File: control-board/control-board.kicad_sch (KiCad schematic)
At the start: 623 parts, among them J1 LED ch 1-24, J10 ESP32 left (3V3 row), J11 ESP32 right (GND row), J2 LED ch 25-48, J3 LED ch 49-72, J4 LED ch 73-96, J5 logic/analog, J6 24V IN, J7 24V IN (5.5/2.5), J8 FAN 24V, Q1 AO3400A, SW1 MODE, SW2 UP, SW3 DOWN, U1 PT4115, U10 PT4115, U101 PCA9685PW (0x40), U102 PCA9685PW (0x41), U103 PCA9685PW (0x42), U104 PCA9685PW (0x43), U105 PCA9685PW (0x44), U106 PCA9685PW (0x45), U11 PT4115, U110 XL1509-5.0E1, U111 ADS1115IDGS (DNP), U12 PT4115, U13 PT4115, U14 PT4115, U15 PT4115, U16 PT4115, U17 PT4115, U18 PT4115, U19 PT4115, U2 PT4115, U20 PT4115, U21 PT4115, U22 PT4115, U23 PT4115, U24 PT4115, U25 PT4115, U26 PT4115, U27 PT4115, U28 PT4115, U29 PT4115, U3 PT4115, U30 PT4115, U31 PT4115, U32 PT4115, U33 PT4115, U34 PT4115, U35 PT4115, U36 PT4115, U37 PT4115, U38 PT4115, U39 PT4115, U4 PT4115, U40 PT4115, U41 PT4115, U42 PT4115, U43 PT4115, U44 PT4115, U45 PT4115, U46 PT4115, U47 PT4115, U48 PT4115, U49 PT4115, U5 PT4115, U50 PT4115, U51 PT4115, U52 PT4115, U53 PT4115, U54 PT4115, U55 PT4115, U56 PT4115, U57 PT4115, U58 PT4115, U59 PT4115, U6 PT4115, U60 PT4115, U61 PT4115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

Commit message: Hierarchical schematics: fully wired, netlist-verified, ERC clean
- Root + well.kicad_sch / channel.kicad_sch instantiated 96x each;
  refs preserved (LED1-96, U1-96...) via instance paths
- Sub-sheets pre-wired; root connected via net labels; no_connects
  on unused ESP32 socket pins; PWR_FLAGs per rail
- verify_netlist.py: KiCad netlist export matches design_data on all
  300 (LED) + 412 (control) intended nets; ERC clean / 3 benign warns
- LCSC corrections from verification agent applied (C125847, C134514,
  C286136, C134820, C36414); datasheets for all parts in reference/
- jlc_parts pins normalized to passive

Co-Authored-By: Claude Fable 5 <noreply@anthropic.com>
Claude-Session: https://claude.ai/code/session_017oD54uh7Tvu54u9NPQNcZB
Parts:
- removed C1, C10, C11, C12, C13, C14, C15, C16, C17, C18, C19, C2, C20, C21, C22, C23, C24, C25, C26, C27, C28, C29, C3, C30, C31, C32, C33, C34, C35, C36, C37, C38, C39, C4, C40, C41, C42, C43, C44, C45, C46, C47, C48, C49, C5, C50, C51, C52, C53, C54, C55, C56, C57, C58, C59, C6, C60, C61, C62, C63, C64, C65, C66, C67, C68, C69, C7, C70, C71, C72, C73, C74, C75, C76, C77, C78, C79, C8, C80, C81, C82, C83, C84, C85, C86, C87, C88, C89, C9, C90, C91, C92, C93, C94, C95, C96: 2.2uF 50V, Capacitor_SMD:C_0805_2012Metric, symbol Device:C
- removed D1, D10, D11, D12, D13, D14, D15, D16, D17, D18, D19, D2, D20, D21, D22, D23, D24, D25, D26, D27, D28, D29, D3, D30, D31, D32, D33, D34, D35, D36, D37, D38, D39, D4, D40, D41, D42, D43, D44, D45, D46, D47, D48, D49, D5, D50, D51, D52, D53, D54, D55, D56, D57, D58, D59, D6, D60, D61, D62, D63, D64, D65, D66, D67, D68, D69, D7, D70, D71, D72, D73, D74, D75, D76, D77, D78, D79, D8, D80, D81, D82, D83, D84, D85, D86, D87, D88, D89, D9, D90, D91, D92, D93, D94, D95, D96: SS34, Diode_SMD:D_SMA, symbol Device:D_Schottky
- removed L1, L10, L11, L12, L13, L14, L15, L16, L17, L18, L19, L2, L20, L21, L22, L23, L24, L25, L26, L27, L28, L29, L3, L30, L31, L32, L33, L34, L35, L36, L37, L38, L39, L4, L40, L41, L42, L43, L44, L45, L46, L47, L48, L49, L5, L50, L51, L52, L53, L54, L55, L56, L57, L58, L59, L6, L60, L61, L62, L63, L64, L65, L66, L67, L68, L69, L7, L70, L71, L72, L73, L74, L75, L76, L77, L78, L79, L8, L80, L81, L82, L83, L84, L85, L86, L87, L88, L89, L9, L90, L91, L92, L93, L94, L95, L96: 47uH, Inductor_SMD:L_Sunlord_SWPA4030S, symbol Device:L
- removed R1, R10, R11, R12, R13, R14, R15, R16, R17, R18, R19, R2, R20, R21, R22, R23, R24, R25, R26, R27, R28, R29, R3, R30, R31, R32, R33, R34, R35, R36, R37, R38, R39, R4, R40, R41, R42, R43, R44, R45, R46, R47, R48, R49, R5, R50, R51, R52, R53, R54, R55, R56, R57, R58, R59, R6, R60, R61, R62, R63, R64, R65, R66, R67, R68, R69, R7, R70, R71, R72, R73, R74, R75, R76, R77, R78, R79, R8, R80, R81, R82, R83, R84, R85, R86, R87, R88, R89, R9, R90, R91, R92, R93, R94, R95, R96: 0.39R 1%, Resistor_SMD:R_0805_2012Metric, symbol Device:R
- removed R101, R102, R103, R104, R105, R106, R107, R108, R109, R110, R111, R112, R113, R114, R115, R116, R117, R118, R119, R120, R121, R122, R123, R124, R125, R126, R127, R128, R129, R130, R131, R132, R133, R134, R135, R136, R137, R138, R139, R140, R141, R142, R143, R144, R145, R146, R147, R148, R149, R150, R151, R152, R153, R154, R155, R156, R157, R158, R159, R160, R161, R162, R163, R164, R165, R166, R167, R168, R169, R170, R171, R172, R173, R174, R175, R176, R177, R178, R179, R180, R181, R182, R183, R184, R185, R186, R187, R188, R189, R190, R191, R192, R193, R194, R195, R196: 100k, Resistor_SMD:R_0603_1608Metric, symbol Device:R
- removed U1, U10, U11, U12, U13, U14, U15, U16, U17, U18, U19, U2, U20, U21, U22, U23, U24, U25, U26, U27, U28, U29, U3, U30, U31, U32, U33, U34, U35, U36, U37, U38, U39, U4, U40, U41, U42, U43, U44, U45, U46, U47, U48, U49, U5, U50, U51, U52, U53, U54, U55, U56, U57, U58, U59, U6, U60, U61, U62, U63, U64, U65, U66, U67, U68, U69, U7, U70, U71, U72, U73, U74, U75, U76, U77, U78, U79, U8, U80, U81, U82, U83, U84, U85, U86, U87, U88, U89, U9, U90, U91, U92, U93, U94, U95, U96: PT4115, jlc_parts:SOT-89-5_L4.5-W2.5-P1.50-LS4.5-BR, symbol jlc_parts:PT4115
- C101, C102, C103, C104: LCSC C134728 -> C134820
- C110: LCSC C134722 -> C134514
- C111: LCSC C134727 -> C286136
- J5: footprint Connector_IDC:IDC-Header_2x10_P2.54mm_Vertical -> Connector_IDC:IDC-Header_2x10_P2.54mm_Horizontal
- L101: LCSC C2896384 -> C36414
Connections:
- net BTN_UP: now reaches SW2.1 (A)
- net BTN_UP: now also J10.11 (Pin_11), SW2.2 (B)
- net GND: now reaches SW2.3 (C)
- net GND: now also C101.2, C102.2, C103.2, C104.2, C110.2, C111.2, C121.2, C122.2, C123.2, C124.2, C125.2, C126.2, D101.2 (A), J1.49 (Pin_49), J1.50 (Pin_50), J10.14 (Pin_14), J11.1 (Pin_1), J11.7 (Pin_7), J2.49 (Pin_49), J2.50 (Pin_50), J3.49 (Pin_49), J3.50 (Pin_50), J4.49 (Pin_49), J4.50 (Pin_50), J5.10 (Pin_10), J5.12 (Pin_12), J5.14 (Pin_14), J5.19 (Pin_19), J5.2 (Pin_2), J5.20 (Pin_20), J5.4 (Pin_4), J5.6 (Pin_6), J5.8 (Pin_8), J6.2 (Pin_2), J7.2, LED1.1 (K), LED2.1 (K), LED3.1 (K), Q1.2 (S), R202.2, SW1.3 (C), SW1.4 (D), SW2.4 (D), SW3.3 (C), SW3.4 (D), U101.1 (A0), U101.14 (VSS), U101.2 (A1), U101.23 (~{OE}), U101.24 (A5), U101.25 (EXTCLK), U101.3 (A2), U101.4 (A3), U101.5 (A4), U102.14 (VSS), U102.2 (A1), U102.23 (~{OE}), U102.24 (A5), U102.25 (EXTCLK), U102.3 (A2), U102.4 (A3), U102.5 (A4), U103.1 (A0), U103.14 (VSS), U103.23 (~{OE}), U103.24 (A5), U103.25 (EXTCLK), U103.3 (A2), U103.4 (A3), U103.5 (A4), U104.14 (VSS), U104.23 (~{OE}), U104.24 (A5), U104.25 (EXTCLK), U104.3 (A2), U104.4 (A3), U104.5 (A4), U105.1 (A0), U105.14 (VSS), U105.2 (A1), U105.23 (~{OE}), U105.24 (A5), U105.25 (EXTCLK), U105.4 (A3), U105.5 (A4), U106.14 (VSS), U106.2 (A1), U106.23 (~{OE}), U106.24 (A5), U106.25 (EXTCLK), U106.4 (A3), U106.5 (A4), U110.4 (~{EN}), U110.5 (GND), U110.6 (GND), U110.7 (GND), U110.8 (GND), U111.1 (ADDR), U111.3 (GND)
- net +3V3: now reaches C122.1
- net +3V3: now also C121.1, C123.1, C124.1, C125.1, C126.1, J10.1 (Pin_1), J5.1 (Pin_1), R210.2, R211.2, U101.28 (VDD), U102.1 (A0), U102.28 (VDD), U103.2 (A1), U103.28 (VDD), U104.1 (A0), U104.2 (A1), U104.28 (VDD), U105.28 (VDD), U105.3 (A2), U106.1 (A0), U106.28 (VDD), U106.3 (A2), U111.8 (VDD)
- net +24V: now reaches J6.1 (Pin_1)
- net +24V: now also C101.1, C102.1, C103.1, C104.1, C110.1, D102.1 (K), J7.1, J8.1 (Pin_1), U110.1 (VIN)
- net I2C_SDA: now reaches U111.10 (SCL)
- net I2C_SDA: now also J11.6 (Pin_6), R210.1, U101.27 (SDA), U102.27 (SDA), U103.27 (SDA), U104.27 (SDA), U105.27 (SDA), U106.27 (SDA)
- net I2C_SCL: now reaches U111.9 (SDA)
- net I2C_SCL: now also J11.3 (Pin_3), R211.1, U101.26 (SCL), U102.26 (SCL), U103.26 (SCL), U104.26 (SCL), U105.26 (SCL), U106.26 (SCL)
- net +5V: now reaches R203.1
- net +5V: now also C111.1, J10.19 (Pin_19), L101.2, U110.3 (FB)
- net LED1_A: now reaches R203.2
- net LED1_A: now also LED1.2 (A)
- net FAN_G: now reaches Q1.1 (G)
- net FAN_G: now also R201.2, R202.1
- net FAN_SW: now reaches Q1.3 (D)
- net FAN_SW: now also D102.2 (A), J8.2 (Pin_2)
- net SW_5V: now reaches U110.2 (OUT)
- net SW_5V: now also D101.1 (K), L101.1
- net MUX_A1: now reaches J11.11 (Pin_11)
- net MUX_A1: now also J5.16 (Pin_16)
- net MUX_A0: now reaches J11.12 (Pin_12)
- net MUX_A0: now also J5.15 (Pin_15)
- net LED_STATUS: now reaches J11.13 (Pin_13)
- net LED_STATUS: now also R204.1
- net MUX_A3: now reaches J11.8 (Pin_8)
- net MUX_A3: now also J5.18 (Pin_18)
- net MUX_A2: now reaches J11.9 (Pin_9)
- net MUX_A2: now also J5.17 (Pin_17)
- net FAN_PWM: now reaches R201.1
- net FAN_PWM: now also J10.9 (Pin_9)
- net DIM85: now reaches U106.10 (LED4)
- net DIM86: now reaches U106.11 (LED5)
- net DIM87: now reaches U106.12 (LED6)
- net DIM88: now reaches U106.13 (LED7)
- net DIM89: now reaches U106.15 (LED8)
- net DIM90: now reaches U106.16 (LED9)
- net DIM91: now reaches U106.17 (LED10)
- net DIM92: now reaches U106.18 (LED11)
- net DIM93: now reaches U106.19 (LED12)
- net DIM94: now reaches U106.20 (LED13)
- net DIM95: now reaches U106.21 (LED14)
- net DIM96: now reaches U106.22 (LED15)
- net DIM81: now reaches U106.6 (LED0)
- net DIM82: now reaches U106.7 (LED1)
- net DIM83: now reaches U106.8 (LED2)
- net DIM84: now reaches U106.9 (LED3)
- net NTC_SIG5: now reaches J5.11 (Pin_11)
- net NTC_SIG5: now also J10.3 (Pin_3)
- net NTC_SIG6: now reaches J5.13 (Pin_13)
- net NTC_SIG6: now also J10.4 (Pin_4)
- net NTC_SIG1: now reaches J5.3 (Pin_3)
- net NTC_SIG1: now also J10.7 (Pin_7)
- net NTC_SIG2: now reaches J5.5 (Pin_5)
- net NTC_SIG2: now also J10.8 (Pin_8)
- net NTC_SIG3: now reaches J5.7 (Pin_7)
- net NTC_SIG3: now also J10.5 (Pin_5)
- net NTC_SIG4: now reaches J5.9 (Pin_9)
- net NTC_SIG4: now also J10.6 (Pin_6)
- net LED_FAULT: now reaches R205.1
- net LED_FAULT: now also J10.15 (Pin_15)
- net LED3_A: now reaches R205.2
- net LED3_A: now also LED3.2 (A)
- net LED2_A: now reaches R204.2
- net LED2_A: now also LED2.2 (A)
- net LED_A49: now reaches J3.1 (Pin_1)
- net LED_K53: now reaches J3.10 (Pin_10)
- net LED_A54: now reaches J3.11 (Pin_11)
- net LED_K54: now reaches J3.12 (Pin_12)
- net LED_A55: now reaches J3.13 (Pin_13)
- net LED_K55: now reaches J3.14 (Pin_14)
- net LED_A56: now reaches J3.15 (Pin_15)
- net LED_K56: now reaches J3.16 (Pin_16)
- net LED_A57: now reaches J3.17 (Pin_17)
- net LED_K57: now reaches J3.18 (Pin_18)
- net LED_A58: now reaches J3.19 (Pin_19)
- net LED_K49: now reaches J3.2 (Pin_2)
- net LED_K58: now reaches J3.20 (Pin_20)
- net LED_A59: now reaches J3.21 (Pin_21)
- net LED_K59: now reaches J3.22 (Pin_22)
- net LED_A60: now reaches J3.23 (Pin_23)
- net LED_K60: now reaches J3.24 (Pin_24)
- net LED_A61: now reaches J3.25 (Pin_25)
- net LED_K61: now reaches J3.26 (Pin_26)
- net LED_A62: now reaches J3.27 (Pin_27)
- net LED_K62: now reaches J3.28 (Pin_28)
- net LED_A63: now reaches J3.29 (Pin_29)
- net LED_A50: now reaches J3.3 (Pin_3)
- net LED_K63: now reaches J3.30 (Pin_30)
- net LED_A64: now reaches J3.31 (Pin_31)
- net LED_K64: now reaches J3.32 (Pin_32)
- net LED_A65: now reaches J3.33 (Pin_33)
- net LED_K65: now reaches J3.34 (Pin_34)
- net LED_A66: now reaches J3.35 (Pin_35)
- net LED_K66: now reaches J3.36 (Pin_36)
- net LED_A67: now reaches J3.37 (Pin_37)
- net LED_K67: now reaches J3.38 (Pin_38)
- net LED_A68: now reaches J3.39 (Pin_39)
- net LED_K50: now reaches J3.4 (Pin_4)
- net LED_K68: now reaches J3.40 (Pin_40)
- net LED_A69: now reaches J3.41 (Pin_41)
- net LED_K69: now reaches J3.42 (Pin_42)
- net LED_A70: now reaches J3.43 (Pin_43)
- net LED_K70: now reaches J3.44 (Pin_44)
- net LED_A71: now reaches J3.45 (Pin_45)
- net LED_K71: now reaches J3.46 (Pin_46)
- net LED_A72: now reaches J3.47 (Pin_47)
- net LED_K72: now reaches J3.48 (Pin_48)
- net LED_A51: now reaches J3.5 (Pin_5)
- net LED_K51: now reaches J3.6 (Pin_6)
- net LED_A52: now reaches J3.7 (Pin_7)
- net LED_K52: now reaches J3.8 (Pin_8)
- net LED_A53: now reaches J3.9 (Pin_9)
- net DIM21: now reaches U102.10 (LED4)
- net DIM22: now reaches U102.11 (LED5)
- net DIM23: now reaches U102.12 (LED6)
- net DIM24: now reaches U102.13 (LED7)
- net DIM25: now reaches U102.15 (LED8)
- net DIM26: now reaches U102.16 (LED9)
- net DIM27: now reaches U102.17 (LED10)
- net DIM28: now reaches U102.18 (LED11)
- net DIM29: now reaches U102.19 (LED12)
- net DIM30: now reaches U102.20 (LED13)
- net DIM31: now reaches U102.21 (LED14)
- net DIM32: now reaches U102.22 (LED15)
- net DIM17: now reaches U102.6 (LED0)
- net DIM18: now reaches U102.7 (LED1)
- net DIM19: now reaches U102.8 (LED2)
- net DIM20: now reaches U102.9 (LED3)
- net LED_A25: now reaches J2.1 (Pin_1)
- net LED_K29: now reaches J2.10 (Pin_10)
- net LED_A30: now reaches J2.11 (Pin_11)
- net LED_K30: now reaches J2.12 (Pin_12)
- net LED_A31: now reaches J2.13 (Pin_13)
- net LED_K31: now reaches J2.14 (Pin_14)
- net LED_A32: now reaches J2.15 (Pin_15)
- net LED_K32: now reaches J2.16 (Pin_16)
- net LED_A33: now reaches J2.17 (Pin_17)
- net LED_K33: now reaches J2.18 (Pin_18)
- net LED_A34: now reaches J2.19 (Pin_19)
- net LED_K25: now reaches J2.2 (Pin_2)
- net LED_K34: now reaches J2.20 (Pin_20)
- net LED_A35: now reaches J2.21 (Pin_21)
- net LED_K35: now reaches J2.22 (Pin_22)
- net LED_A36: now reaches J2.23 (Pin_23)
- net LED_K36: now reaches J2.24 (Pin_24)
- net LED_A37: now reaches J2.25 (Pin_25)
- net LED_K37: now reaches J2.26 (Pin_26)
- net LED_A38: now reaches J2.27 (Pin_27)
- net LED_K38: now reaches J2.28 (Pin_28)
- net LED_A39: now reaches J2.29 (Pin_29)
- net LED_A26: now reaches J2.3 (Pin_3)
- net LED_K39: now reaches J2.30 (Pin_30)
- net LED_A40: now reaches J2.31 (Pin_31)
- net LED_K40: now reaches J2.32 (Pin_32)
- net LED_A41: now reaches J2.33 (Pin_33)
- net LED_K41: now reaches J2.34 (Pin_34)
- net LED_A42: now reaches J2.35 (Pin_35)
- net LED_K42: now reaches J2.36 (Pin_36)
- net LED_A43: now reaches J2.37 (Pin_37)
- net LED_K43: now reaches J2.38 (Pin_38)
- net LED_A44: now reaches J2.39 (Pin_39)
- net LED_K26: now reaches J2.4 (Pin_4)
- net LED_K44: now reaches J2.40 (Pin_40)
- net LED_A45: now reaches J2.41 (Pin_41)
- net LED_K45: now reaches J2.42 (Pin_42)
- net LED_A46: now reaches J2.43 (Pin_43)
- net LED_K46: now reaches J2.44 (Pin_44)
- net LED_A47: now reaches J2.45 (Pin_45)
- net LED_K47: now reaches J2.46 (Pin_46)
- net LED_A48: now reaches J2.47 (Pin_47)
- net LED_K48: now reaches J2.48 (Pin_48)
- net LED_A27: now reaches J2.5 (Pin_5)
- net LED_K27: now reaches J2.6 (Pin_6)
- net LED_A28: now reaches J2.7 (Pin_7)
- net LED_K28: now reaches J2.8 (Pin_8)
- net LED_A29: now reaches J2.9 (Pin_9)
- net BTN_DOWN: now reaches J10.10 (Pin_10)
- net BTN_DOWN: now also SW3.1 (A), SW3.2 (B)
- net BTN_MODE: now reaches J10.12 (Pin_12)
- net BTN_MODE: now also SW1.1 (A), SW1.2 (B)
- net DIM53: now reaches U104.10 (LED4)
- net DIM54: now reaches U104.11 (LED5)
- net DIM55: now reaches U104.12 (LED6)
- net DIM56: now reaches U104.13 (LED7)
- net DIM57: now reaches U104.15 (LED8)
- net DIM58: now reaches U104.16 (LED9)
- net DIM59: now reaches U104.17 (LED10)
- net DIM60: now reaches U104.18 (LED11)
- net DIM61: now reaches U104.19 (LED12)
- net DIM62: now reaches U104.20 (LED13)
- net DIM63: now reaches U104.21 (LED14)
- net DIM64: now reaches U104.22 (LED15)
- net DIM49: now reaches U104.6 (LED0)
- net DIM50: now reaches U104.7 (LED1)
- net DIM51: now reaches U104.8 (LED2)
- net DIM52: now reaches U104.9 (LED3)
- net LED_A73: now reaches J4.1 (Pin_1)
- net LED_K77: now reaches J4.10 (Pin_10)
- net LED_A78: now reaches J4.11 (Pin_11)
- net LED_K78: now reaches J4.12 (Pin_12)
- net LED_A79: now reaches J4.13 (Pin_13)
- net LED_K79: now reaches J4.14 (Pin_14)
- net LED_A80: now reaches J4.15 (Pin_15)
- net LED_K80: now reaches J4.16 (Pin_16)
- net LED_A81: now reaches J4.17 (Pin_17)
- net LED_K81: now reaches J4.18 (Pin_18)
- net LED_A82: now reaches J4.19 (Pin_19)
- net LED_K73: now reaches J4.2 (Pin_2)
- net LED_K82: now reaches J4.20 (Pin_20)
- net LED_A83: now reaches J4.21 (Pin_21)
- net LED_K83: now reaches J4.22 (Pin_22)
- net LED_A84: now reaches J4.23 (Pin_23)
- net LED_K84: now reaches J4.24 (Pin_24)
- net LED_A85: now reaches J4.25 (Pin_25)
- net LED_K85: now reaches J4.26 (Pin_26)
- net LED_A86: now reaches J4.27 (Pin_27)
- net LED_K86: now reaches J4.28 (Pin_28)
- net LED_A87: now reaches J4.29 (Pin_29)
- net LED_A74: now reaches J4.3 (Pin_3)
- net LED_K87: now reaches J4.30 (Pin_30)
- net LED_A88: now reaches J4.31 (Pin_31)
- net LED_K88: now reaches J4.32 (Pin_32)
- net LED_A89: now reaches J4.33 (Pin_33)
- net LED_K89: now reaches J4.34 (Pin_34)
- net LED_A90: now reaches J4.35 (Pin_35)
- net LED_K90: now reaches J4.36 (Pin_36)
- net LED_A91: now reaches J4.37 (Pin_37)
- net LED_K91: now reaches J4.38 (Pin_38)
- net LED_A92: now reaches J4.39 (Pin_39)
- net LED_K74: now reaches J4.4 (Pin_4)
- net LED_K92: now reaches J4.40 (Pin_40)
- net LED_A93: now reaches J4.41 (Pin_41)
- net LED_K93: now reaches J4.42 (Pin_42)
- net LED_A94: now reaches J4.43 (Pin_43)
- net LED_K94: now reaches J4.44 (Pin_44)
- net LED_A95: now reaches J4.45 (Pin_45)
- net LED_K95: now reaches J4.46 (Pin_46)
- net LED_A96: now reaches J4.47 (Pin_47)
- net LED_K96: now reaches J4.48 (Pin_48)
- net LED_A75: now reaches J4.5 (Pin_5)
- net LED_K75: now reaches J4.6 (Pin_6)
- net LED_A76: now reaches J4.7 (Pin_7)
- net LED_K76: now reaches J4.8 (Pin_8)
- net LED_A77: now reaches J4.9 (Pin_9)
- net DIM37: now reaches U103.10 (LED4)
- net DIM38: now reaches U103.11 (LED5)
- net DIM39: now reaches U103.12 (LED6)
- net DIM40: now reaches U103.13 (LED7)
- net DIM41: now reaches U103.15 (LED8)
- net DIM42: now reaches U103.16 (LED9)
- net DIM43: now reaches U103.17 (LED10)
- net DIM44: now reaches U103.18 (LED11)
- net DIM45: now reaches U103.19 (LED12)
- net DIM46: now reaches U103.20 (LED13)
- net DIM47: now reaches U103.21 (LED14)
- net DIM48: now reaches U103.22 (LED15)
- net DIM33: now reaches U103.6 (LED0)
- net DIM34: now reaches U103.7 (LED1)
- net DIM35: now reaches U103.8 (LED2)
- net DIM36: now reaches U103.9 (LED3)
- net DIM69: now reaches U105.10 (LED4)
- net DIM70: now reaches U105.11 (LED5)
- net DIM71: now reaches U105.12 (LED6)
- net DIM72: now reaches U105.13 (LED7)
- net DIM73: now reaches U105.15 (LED8)
- net DIM74: now reaches U105.16 (LED9)
- net DIM75: now reaches U105.17 (LED10)
- net DIM76: now reaches U105.18 (LED11)
- net DIM77: now reaches U105.19 (LED12)
- net DIM78: now reaches U105.20 (LED13)
- net DIM79: now reaches U105.21 (LED14)
- net DIM80: now reaches U105.22 (LED15)
- net DIM65: now reaches U105.6 (LED0)
- net DIM66: now reaches U105.7 (LED1)
- net DIM67: now reaches U105.8 (LED2)
- net DIM68: now reaches U105.9 (LED3)
- net DIM5: now reaches U101.10 (LED4)
- net DIM6: now reaches U101.11 (LED5)
- net DIM7: now reaches U101.12 (LED6)
- net DIM8: now reaches U101.13 (LED7)
- net DIM9: now reaches U101.15 (LED8)
- net DIM10: now reaches U101.16 (LED9)
- net DIM11: now reaches U101.17 (LED10)
- net DIM12: now reaches U101.18 (LED11)
- net DIM13: now reaches U101.19 (LED12)
- net DIM14: now reaches U101.20 (LED13)
- net DIM15: now reaches U101.21 (LED14)
- net DIM16: now reaches U101.22 (LED15)
- net DIM1: now reaches U101.6 (LED0)
- net DIM2: now reaches U101.7 (LED1)
- net DIM3: now reaches U101.8 (LED2)
- net DIM4: now reaches U101.9 (LED3)
- net LED_A1: now reaches J1.1 (Pin_1)
- net LED_K5: now reaches J1.10 (Pin_10)
- net LED_A6: now reaches J1.11 (Pin_11)
- net LED_K6: now reaches J1.12 (Pin_12)
- net LED_A7: now reaches J1.13 (Pin_13)
- net LED_K7: now reaches J1.14 (Pin_14)
- net LED_A8: now reaches J1.15 (Pin_15)
- net LED_K8: now reaches J1.16 (Pin_16)
- net LED_A9: now reaches J1.17 (Pin_17)
- net LED_K9: now reaches J1.18 (Pin_18)
- net LED_A10: now reaches J1.19 (Pin_19)
- net LED_K1: now reaches J1.2 (Pin_2)
- net LED_K10: now reaches J1.20 (Pin_20)
- net LED_A11: now reaches J1.21 (Pin_21)
- net LED_K11: now reaches J1.22 (Pin_22)
- net LED_A12: now reaches J1.23 (Pin_23)
- net LED_K12: now reaches J1.24 (Pin_24)
- net LED_A13: now reaches J1.25 (Pin_25)
- net LED_K13: now reaches J1.26 (Pin_26)
- net LED_A14: now reaches J1.27 (Pin_27)
- net LED_K14: now reaches J1.28 (Pin_28)
- net LED_A15: now reaches J1.29 (Pin_29)
- net LED_A2: now reaches J1.3 (Pin_3)
- net LED_K15: now reaches J1.30 (Pin_30)
- net LED_A16: now reaches J1.31 (Pin_31)
- net LED_K16: now reaches J1.32 (Pin_32)
- net LED_A17: now reaches J1.33 (Pin_33)
- net LED_K17: now reaches J1.34 (Pin_34)
- net LED_A18: now reaches J1.35 (Pin_35)
- net LED_K18: now reaches J1.36 (Pin_36)
- net LED_A19: now reaches J1.37 (Pin_37)
- net LED_K19: now reaches J1.38 (Pin_38)
- net LED_A20: now reaches J1.39 (Pin_39)
- net LED_K2: now reaches J1.4 (Pin_4)
- net LED_K20: now reaches J1.40 (Pin_40)
- net LED_A21: now reaches J1.41 (Pin_41)
- net LED_K21: now reaches J1.42 (Pin_42)
- net LED_A22: now reaches J1.43 (Pin_43)
- net LED_K22: now reaches J1.44 (Pin_44)
- net LED_A23: now reaches J1.45 (Pin_45)
- net LED_K23: now reaches J1.46 (Pin_46)
- net LED_A24: now reaches J1.47 (Pin_47)
- net LED_K24: now reaches J1.48 (Pin_48)
- net LED_A3: now reaches J1.5 (Pin_5)
- net LED_K3: now reaches J1.6 (Pin_6)
- net LED_A4: now reaches J1.7 (Pin_7)
- net LED_K4: now reaches J1.8 (Pin_8)
- net LED_A5: now reaches J1.9 (Pin_9)
- no-connect marks 0 -> 20
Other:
- added sheet CH01 (channel.kicad_sch)
- added sheet CH02 (channel.kicad_sch)
- added sheet CH03 (channel.kicad_sch)
- added sheet CH04 (channel.kicad_sch)
- added sheet CH05 (channel.kicad_sch)
- added sheet CH06 (channel.kicad_sch)
- added sheet CH07 (channel.kicad_sch)
- added sheet CH08 (channel.kicad_sch)
- added sheet CH09 (channel.kicad_sch)
- added sheet CH10 (channel.kicad_sch)
- added sheet CH11 (channel.kicad_sch)
- added sheet CH12 (channel.kicad_sch)
- added sheet CH13 (channel.kicad_sch)
- added sheet CH14 (channel.kicad_sch)
- added sheet CH15 (channel.kicad_sch)
- added sheet CH16 (channel.kicad_sch)
- added sheet CH17 (channel.kicad_sch)
- added sheet CH18 (channel.kicad_sch)
- added sheet CH19 (channel.kicad_sch)
- added sheet CH20 (channel.kicad_sch)
- added sheet CH21 (channel.kicad_sch)
- added sheet CH22 (channel.kicad_sch)
- added sheet CH23 (channel.kicad_sch)
- added sheet CH24 (channel.kicad_sch)
- added sheet CH25 (channel.kicad_sch)
- added sheet CH26 (channel.kicad_sch)
- added sheet CH27 (channel.kicad_sch)
- added sheet CH28 (channel.kicad_sch)
- added sheet CH29 (channel.kicad_sch)
- added sheet CH30 (channel.kicad_sch)
- added sheet CH31 (channel.kicad_sch)
- added sheet CH32 (channel.kicad_sch)
- added sheet CH33 (channel.kicad_sch)
- added sheet CH34 (channel.kicad_sch)
- added sheet CH35 (channel.kicad_sch)
- added sheet CH36 (channel.kicad_sch)
- added sheet CH37 (channel.kicad_sch)
- added sheet CH38 (channel.kicad_sch)
- added sheet CH39 (channel.kicad_sch)
- added sheet CH40 (channel.kicad_sch)
- added sheet CH41 (channel.kicad_sch)
- added sheet CH42 (channel.kicad_sch)
- added sheet CH43 (channel.kicad_sch)
- added sheet CH44 (channel.kicad_sch)
- added sheet CH45 (channel.kicad_sch)
- added sheet CH46 (channel.kicad_sch)
- added sheet CH47 (channel.kicad_sch)
- added sheet CH48 (channel.kicad_sch)
- added sheet CH49 (channel.kicad_sch)
- added sheet CH50 (channel.kicad_sch)
- added sheet CH51 (channel.kicad_sch)
- added sheet CH52 (channel.kicad_sch)
- added sheet CH53 (channel.kicad_sch)
- added sheet CH54 (channel.kicad_sch)
- added sheet CH55 (channel.kicad_sch)
- added sheet CH56 (channel.kicad_sch)
- added sheet CH57 (channel.kicad_sch)
- added sheet CH58 (channel.kicad_sch)
- added sheet CH59 (channel.kicad_sch)
- added sheet CH60 (channel.kicad_sch)
- added sheet CH61 (channel.kicad_sch)
- added sheet CH62 (channel.kicad_sch)
- added sheet CH63 (channel.kicad_sch)
- added sheet CH64 (channel.kicad_sch)
- added sheet CH65 (channel.kicad_sch)
- added sheet CH66 (channel.kicad_sch)
- added sheet CH67 (channel.kicad_sch)
- added sheet CH68 (channel.kicad_sch)
- added sheet CH69 (channel.kicad_sch)
- added sheet CH70 (channel.kicad_sch)
- added sheet CH71 (channel.kicad_sch)
- added sheet CH72 (channel.kicad_sch)
- added sheet CH73 (channel.kicad_sch)
- added sheet CH74 (channel.kicad_sch)
- added sheet CH75 (channel.kicad_sch)
- added sheet CH76 (channel.kicad_sch)
- added sheet CH77 (channel.kicad_sch)
- added sheet CH78 (channel.kicad_sch)
- added sheet CH79 (channel.kicad_sch)
- added sheet CH80 (channel.kicad_sch)
- added sheet CH81 (channel.kicad_sch)
- added sheet CH82 (channel.kicad_sch)
- added sheet CH83 (channel.kicad_sch)
- added sheet CH84 (channel.kicad_sch)
- added sheet CH85 (channel.kicad_sch)
- added sheet CH86 (channel.kicad_sch)
- added sheet CH87 (channel.kicad_sch)
- added sheet CH88 (channel.kicad_sch)
- added sheet CH89 (channel.kicad_sch)
- added sheet CH90 (channel.kicad_sch)
- added sheet CH91 (channel.kicad_sch)
- added sheet CH92 (channel.kicad_sch)
- added sheet CH93 (channel.kicad_sch)
- added sheet CH94 (channel.kicad_sch)
- added sheet CH95 (channel.kicad_sch)
- added sheet CH96 (channel.kicad_sch)
- note added: "5V RAIL + 24V INPUT"
- note added: "96 DRIVER CHANNELS (CH01..CH96) - see channel.kicad_sch"
- note added: "ESP32 DEVKITC-38 SOCKET (J10 left / J11 right, pin1 = 3V3/GND end)"
- note added: "PCA9685 PWM BANK 0x40-0x45"
- note added: "UI"
- note removed: "5V RAIL + 24V INPUT + BULK"
- note removed: "CH1"
- note removed: "CH10"
- note removed: "CH11"
- note removed: "CH12"
- note removed: "CH13"
- note removed: "CH14"
- note removed: "CH15"
- note removed: "CH16"
- note removed: "CH17"
- note removed: "CH18"
- note removed: "CH19"
- note removed: "CH2"
- note removed: "CH20"
- note removed: "CH21"
- note removed: "CH22"
- note removed: "CH23"
- note removed: "CH24"
- note removed: "CH25"
- note removed: "CH26"
- note removed: "CH27"
- note removed: "CH28"
- note removed: "CH29"
- note removed: "CH3"
- note removed: "CH30"
- note removed: "CH31"
- note removed: "CH32"
- note removed: "CH33"
- note removed: "CH34"
- note removed: "CH35"
- note removed: "CH36"
- note removed: "CH37"
- note removed: "CH38"
- note removed: "CH39"
- note removed: "CH4"
- note removed: "CH40"
- note removed: "CH41"
- note removed: "CH42"
- note removed: "CH43"
- note removed: "CH44"
- note removed: "CH45"
- note removed: "CH46"
- note removed: "CH47"
- note removed: "CH48"
- note removed: "CH49"
- note removed: "CH5"
- note removed: "CH50"
- note removed: "CH51"
- note removed: "CH52"
- note removed: "CH53"
- note removed: "CH54"
- note removed: "CH55"
- note removed: "CH56"
- note removed: "CH57"
- note removed: "CH58"
- note removed: "CH59"
- note removed: "CH6"
- note removed: "CH60"
- note removed: "CH61"
- note removed: "CH62"
- note removed: "CH63"
- note removed: "CH64"
- note removed: "CH65"
- note removed: "CH66"
- note removed: "CH67"
- note removed: "CH68"
- note removed: "CH69"
- note removed: "CH7"
- note removed: "CH70"
- note removed: "CH71"
- note removed: "CH72"
- note removed: "CH73"
- note removed: "CH74"
- note removed: "CH75"
- note removed: "CH76"
- note removed: "CH77"
- note removed: "CH78"
- note removed: "CH79"
- note removed: "CH8"
- note removed: "CH80"
- note removed: "CH81"
- note removed: "CH82"
- note removed: "CH83"
- note removed: "CH84"
- note removed: "CH85"
- note removed: "CH86"
- note removed: "CH87"
- note removed: "CH88"
- note removed: "CH89"
- note removed: "CH9"
- note removed: "CH90"
- note removed: "CH91"
- note removed: "CH92"
- note removed: "CH93"
- note removed: "CH94"
- note removed: "CH95"
- note removed: "CH96"
- note removed: "ESP32 DEVKITC-38 SOCKET"
- note removed: "PCA9685 PWM BANK (0x40-0x45)"
- note removed: "UI: BUTTONS + STATUS LEDS"
- note removed: "Wire per CONNECTIONS.md - one PT4115 buck per LED, channel n = row-major (row-1)*12+col"

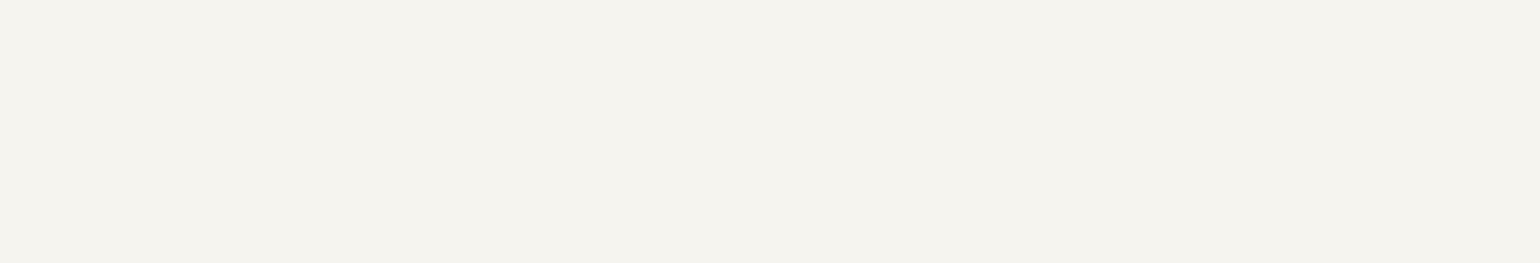
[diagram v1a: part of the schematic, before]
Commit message: Add test points and mounting holes to schematics
- LED board: TP1-TP3 (+3V3, GND x2); H1-H5 as Mechanical:MountingHole
- Control board: TP1-TP12 (rails, SW_5V, I2C, FAN_SW, CH1 debug set
  DIM1/LED_A1/LED_K1); H1-H4
- 1.5mm bare-pad TestPoint footprints (no BOM cost)
- Netlist re-verified: all nets match; ERC still clean

Co-Authored-By: Claude Fable 5 <noreply@anthropic.com>
Claude-Session: https://claude.ai/code/session_017oD54uh7Tvu54u9NPQNcZB
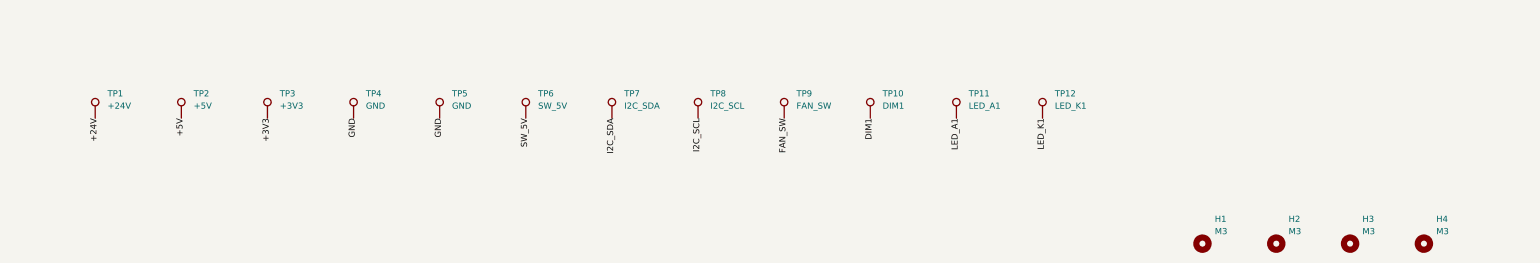
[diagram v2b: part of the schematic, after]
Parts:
- added H1, H2, H3, H4: M3, MountingHole:MountingHole_3.2mm_M3, symbol Mechanical:MountingHole
- added TP1: +24V, TestPoint:TestPoint_Pad_1.5x1.5mm, symbol Connector:TestPoint
- added TP10: DIM1, TestPoint:TestPoint_Pad_1.5x1.5mm, symbol Connector:TestPoint
- added TP11: LED_A1, TestPoint:TestPoint_Pad_1.5x1.5mm, symbol Connector:TestPoint
- added TP12: LED_K1, TestPoint:TestPoint_Pad_1.5x1.5mm, symbol Connector:TestPoint
- added TP2: +5V, TestPoint:TestPoint_Pad_1.5x1.5mm, symbol Connector:TestPoint
- added TP3: +3V3, TestPoint:TestPoint_Pad_1.5x1.5mm, symbol Connector:TestPoint
- added TP4, TP5: GND, TestPoint:TestPoint_Pad_1.5x1.5mm, symbol Connector:TestPoint
- added TP6: SW_5V, TestPoint:TestPoint_Pad_1.5x1.5mm, symbol Connector:TestPoint
- added TP7: I2C_SDA, TestPoint:TestPoint_Pad_1.5x1.5mm, symbol Connector:TestPoint
- added TP8: I2C_SCL, TestPoint:TestPoint_Pad_1.5x1.5mm, symbol Connector:TestPoint
- added TP9: FAN_SW, TestPoint:TestPoint_Pad_1.5x1.5mm, symbol Connector:TestPoint
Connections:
- net +24V: now also TP1.1
- net +3V3: now also TP3.1
- net +5V: now also TP2.1
- net DIM1: now also TP10.1
- net FAN_SW: now also TP9.1
- net GND: now also TP4.1, TP5.1
- net I2C_SCL: now also TP8.1
- net I2C_SDA: now also TP7.1
- net LED_A1: now also TP11.1
- net LED_K1: now also TP12.1
- net SW_5V: now also TP6.1

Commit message: Footprint audit: KF301 terminal footprint with 1.4mm drills
Agent audit verified every footprint pad-for-pad against JLCPCB/EasyEDA
package data; only fix needed was the KF301-5.0-2P screw terminal
(stock MX126 footprint has 1.3mm drills, JLC recommends 1.4mm for the
KF301 blade pins). New footprint in libraries/jlc_parts.pretty;
schematics regenerated; netlist verification still passes on all nets.
Full audit report in reference/datasheets/PART_VERIFICATION.json.

Co-Authored-By: Claude Fable 5 <noreply@anthropic.com>
Claude-Session: https://claude.ai/code/session_017oD54uh7Tvu54u9NPQNcZB
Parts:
- J6: footprint TerminalBlock:TerminalBlock_MaiXu_MX126-5.0-02P_1x02_P5.00mm -> jlc_parts:TerminalBlock_KF301-5.0-2P_1x02_P5.00mm
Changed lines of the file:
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@@
 			)
 		)
-		(property "Footprint" "TerminalBlock:TerminalBlock_MaiXu_MX126-5.0-02P_1x02_P5.00mm"
+		(property "Footprint" "jlc_parts:TerminalBlock_KF301-5.0-2P_1x02_P5.00mm"
 			(at 284.48 448.31 0)
 			(effects

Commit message: Fix 3.3V/GND bridge, adopt +3.3V naming, power symbols at rail pins
- Removed 6 wire segments that tied each mux VCC run into its
  decoupling cap's GND pin (merged the rails through all six caps)
- Renamed +3V3 -> +3.3V everywhere (user convention), incl. well
  sub-sheet power symbols and docs
- Control board root now uses real power symbols on wire stubs
  instead of text labels for GND/+3.3V/+5V/+24V (user style)
- Verified: netlists match design intent on all 300+412 nets; LED
  board ERC 0 violations; I2C addresses confirmed from netlist
  (PCA9685 0x40-0x45, ADS1115 0x48, no conflicts)

Co-Authored-By: Claude Fable 5 <noreply@anthropic.com>
Claude-Session: https://claude.ai/code/session_017oD54uh7Tvu54u9NPQNcZB
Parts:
- TP3: value +3V3 -> +3.3V
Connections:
- net +3V3 renamed +3.3V
